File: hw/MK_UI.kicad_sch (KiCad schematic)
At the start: 19 parts, among them J11 Conn_01x03, J12 Conn_01x30, J13 Conn_02x15_Odd_Even, J14 Conn_01x06, SW1 SP-1, SW1 SP-2

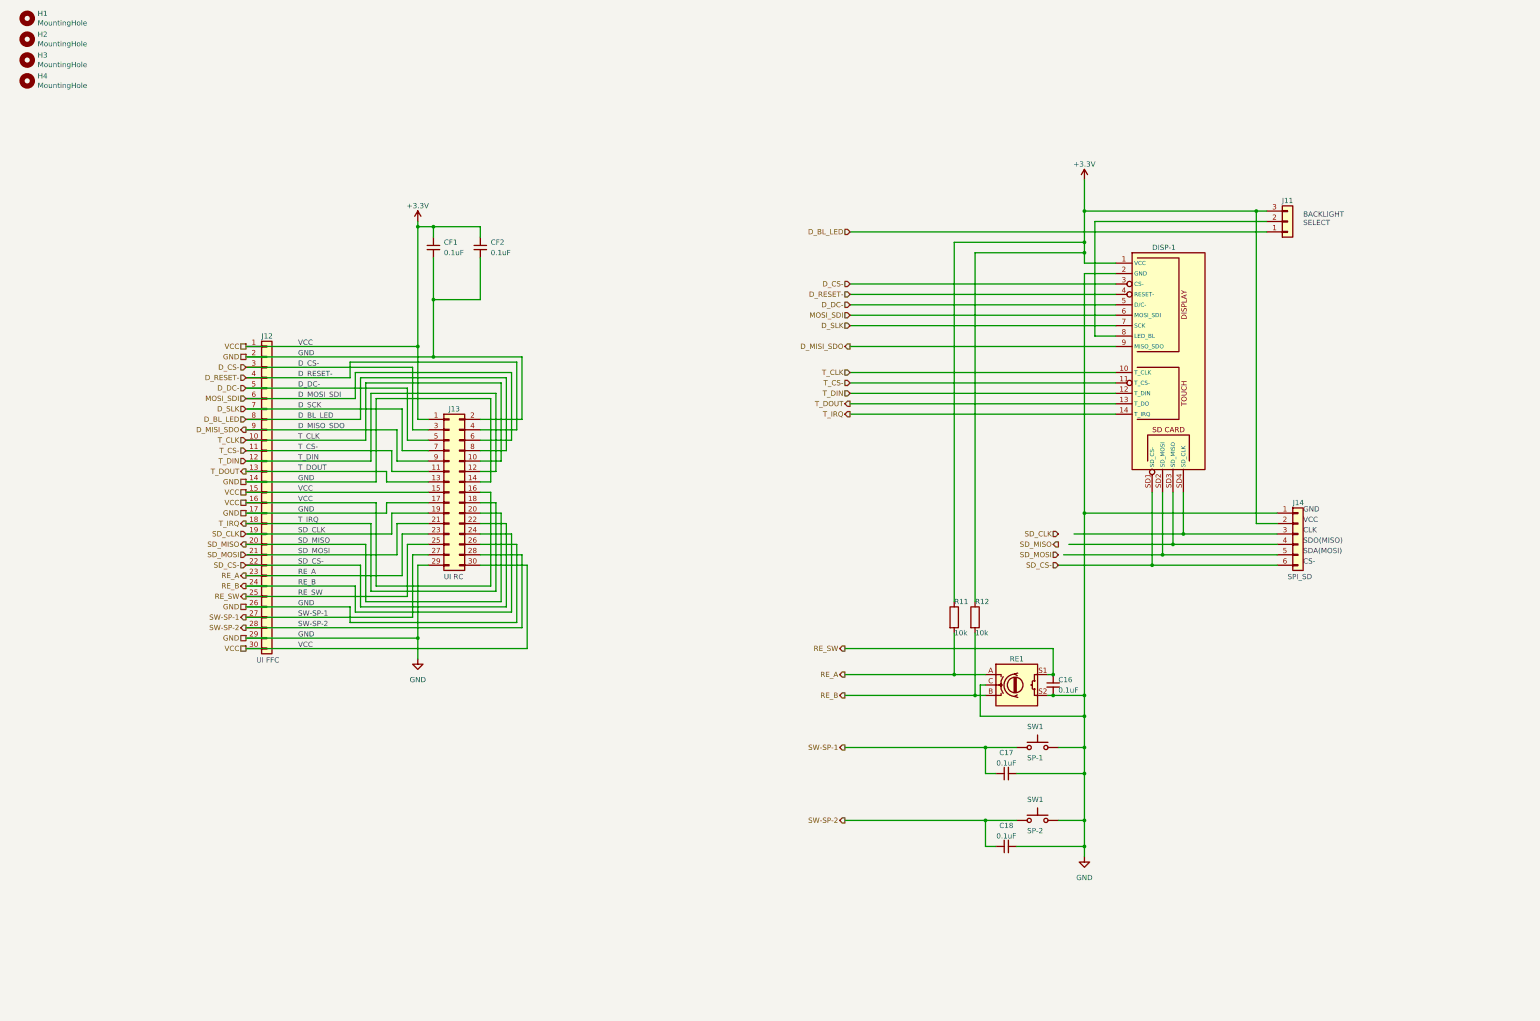
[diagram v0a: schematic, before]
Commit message: Change display backlight GPIO.
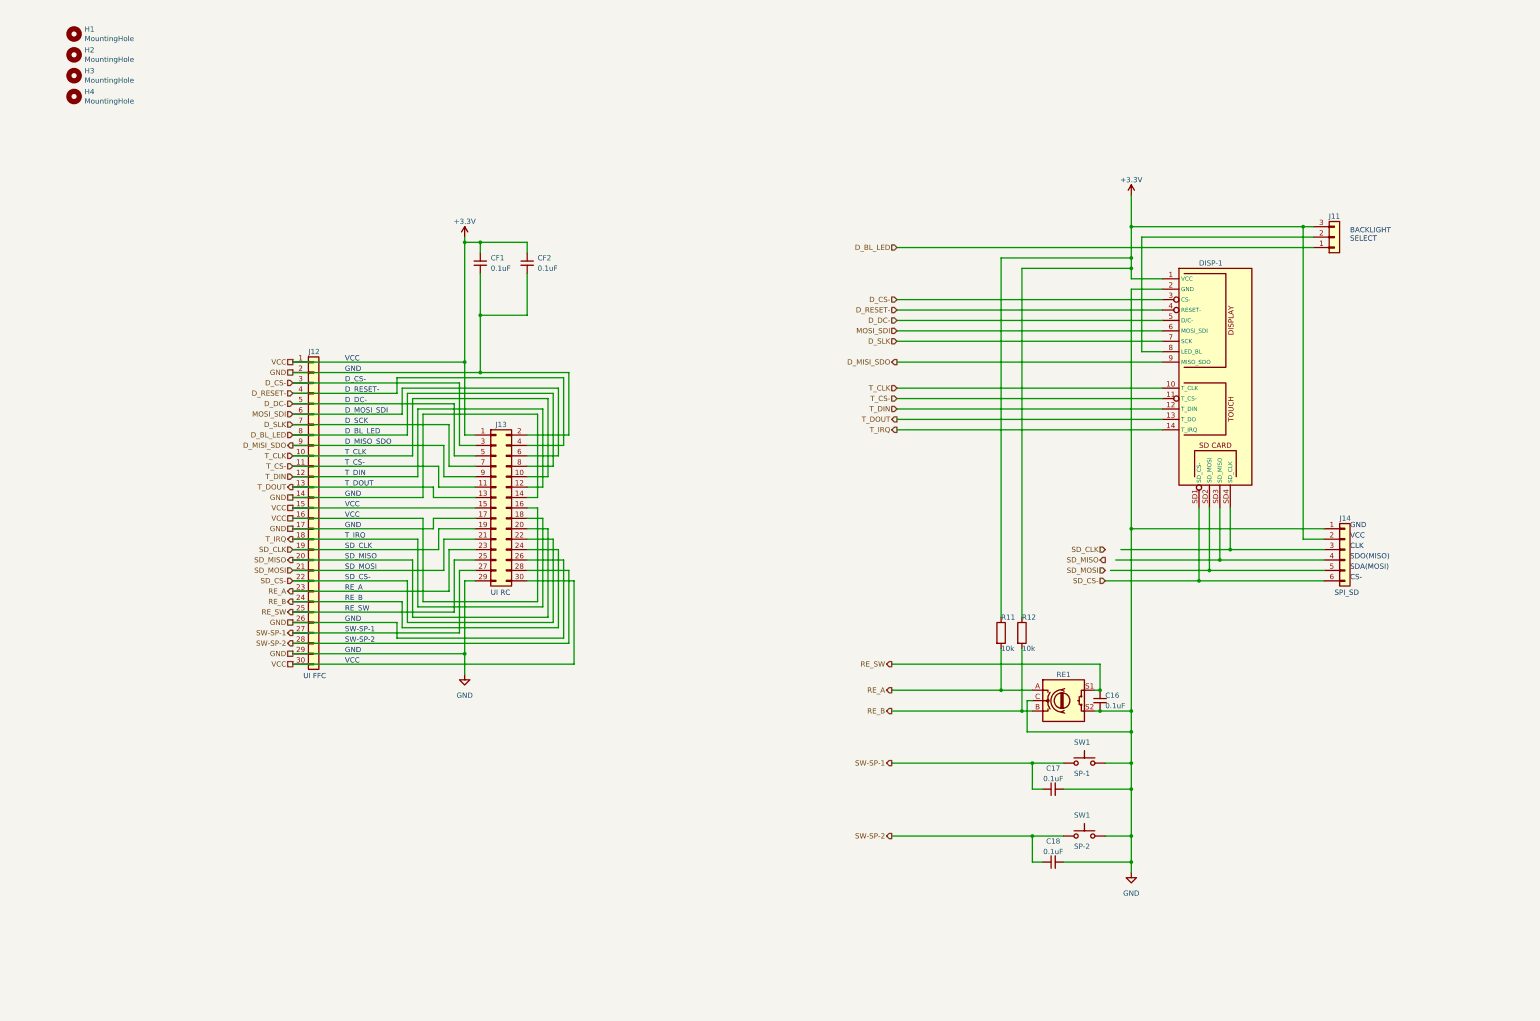
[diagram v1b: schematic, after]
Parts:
- removed SW1: SP-2, Button_Switch_SMD:SW_Push_1P1T_NO_Vertical_Wuerth_434133025816, symbol Switch:SW_Push
- removed SW1: SP-1, Button_Switch_SMD:SW_Push_1P1T_NO_Vertical_Wuerth_434133025816, symbol Switch:SW_Push
- added SW1: SP-2, Button_Switch_SMD:SW_Push_1P1T_NO_Vertical_Wuerth_434133025816, symbol Switch:SW_Push
- added SW1: SP-1, Button_Switch_SMD:SW_Push_1P1T_NO_Vertical_Wuerth_434133025816, symbol Switch:SW_Push
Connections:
- net GND: now also SW1.2, SW1.2
- net SW-SP-1: now also SW1.1
- net SW-SP-2: now also SW1.1
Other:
- title: MuKOB - User Interface -> MuKOB - UI Board

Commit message: Audio on main page. KeySounder Intf on separate board. Switch matrix via Resistors.
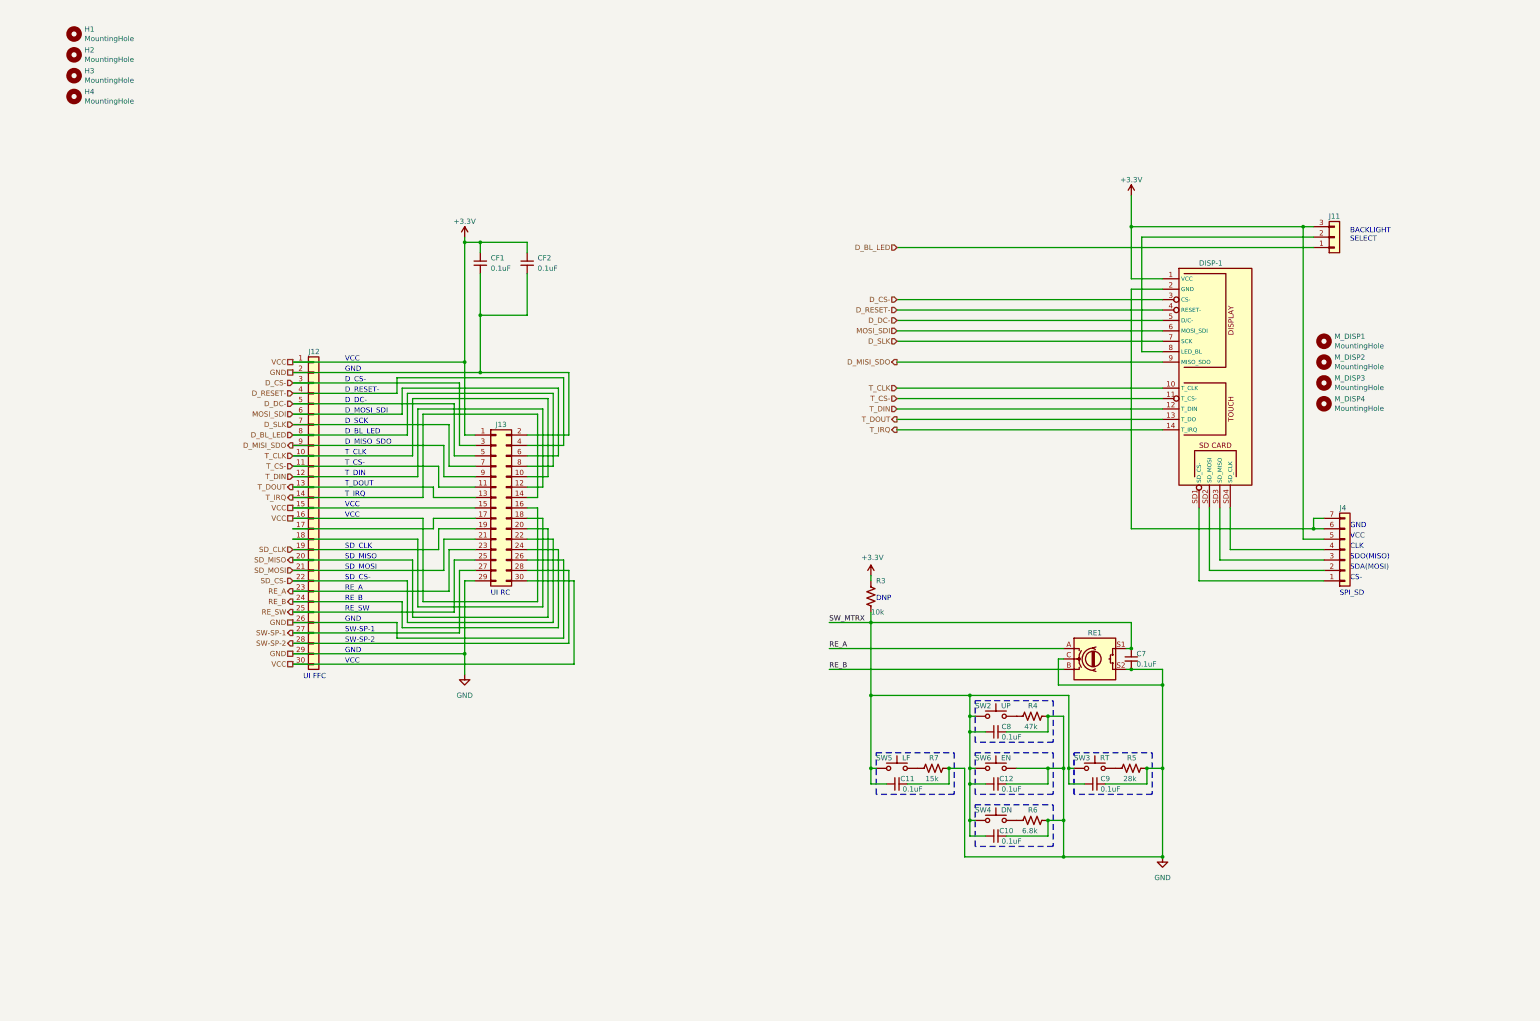
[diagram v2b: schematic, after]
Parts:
- removed C16, C17, C18: 0.1uF, symbol Device:C_Small
- removed J14: Conn_01x06, symbol Connector_Generic:Conn_01x06
- removed R11, R12: 10k, symbol Device:R
- removed SW1: SP-2, Button_Switch_SMD:SW_Push_1P1T_NO_Vertical_Wuerth_434133025816, symbol Switch:SW_Push
- removed SW1: SP-1, Button_Switch_SMD:SW_Push_1P1T_NO_Vertical_Wuerth_434133025816, symbol Switch:SW_Push
- added C10, C11, C12, C7, C8, C9: 0.1uF, symbol Device:C_Small
- added J4: Conn_01x07, symbol Connector_Generic:Conn_01x07
- added M_DISP1, M_DISP2, M_DISP3, M_DISP4: MountingHole, MountingHole:MountingHole_2.7mm_M2.5, symbol Mechanical:MountingHole
- added R3: 10k, symbol Device:R_US
- added R4: 47k, symbol Device:R_US
- added R5: 28k, symbol Device:R_US
- added R6: 6.8k, symbol Device:R_US
- added R7: 15k, symbol Device:R_US
- added SW2: UP, Button_Switch_SMD:SW_Push_1P1T_NO_Vertical_Wuerth_434133025816, symbol Switch:SW_Push
- added SW3: RT, Button_Switch_SMD:SW_Push_1P1T_NO_Vertical_Wuerth_434133025816, symbol Switch:SW_Push
- added SW4: DN, Button_Switch_SMD:SW_Push_1P1T_NO_Vertical_Wuerth_434133025816, symbol Switch:SW_Push
- added SW5: LF, Button_Switch_SMD:SW_Push_1P1T_NO_Vertical_Wuerth_434133025816, symbol Switch:SW_Push
- added SW6: EN, Button_Switch_SMD:SW_Push_1P1T_NO_Vertical_Wuerth_434133025816, symbol Switch:SW_Push
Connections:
- net +3.3V: now also J4.5 (Pin_5), R3.1
- net GND: now also C10.2, C11.2, C12.2, C7.2, C8.2, C9.2, R4.1, R5.1, R6.1, R7.1, SW6.2; no longer DISP-1.2 (GND), J12.14 (Pin_14), J12.17 (Pin_17), J13.14 (Pin_14), J13.17 (Pin_17)
- net RE_SW: no longer RE1.S1
- net SD_CS-: no longer DISP-1.SD1 (SD_CS-)
- net T_IRQ: now also J12.14 (Pin_14), J13.14 (Pin_14); no longer J12.18 (Pin_18), J13.18 (Pin_18)
- net at DISP-1.SD2 (SD_MOSI): now also J4.2 (Pin_2)
- net at DISP-1.SD3 (SD_MISO): now also J4.3 (Pin_3)
- net at DISP-1.SD4 (SD_CLK): now also J4.4 (Pin_4)
- new net: R6.2, SW4.2
- new net: DISP-1.2 (GND), J4.6 (Pin_6), J4.7 (Pin_7)
- new net: DISP-1.SD1 (SD_CS-), J4.1 (Pin_1)
- new net: R4.2, SW2.2
- new net: R7.2, SW5.2
- new net: J12.17 (Pin_17), J13.17 (Pin_17)
- new net: J12.18 (Pin_18), J13.18 (Pin_18)
- new net: R5.2, SW3.2
- new net SW_MTRX: C10.1, C11.1, C12.1, C7.1, C8.1, C9.1, R3.2, RE1.S1, SW2.1, SW3.1, SW4.1, SW5.1, SW6.1
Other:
- note added: "DNP"
- company: AESilky -> Silky-Design (AESilky)

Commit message: Reorganize onto 3 boards. Use 20pin UI connector.
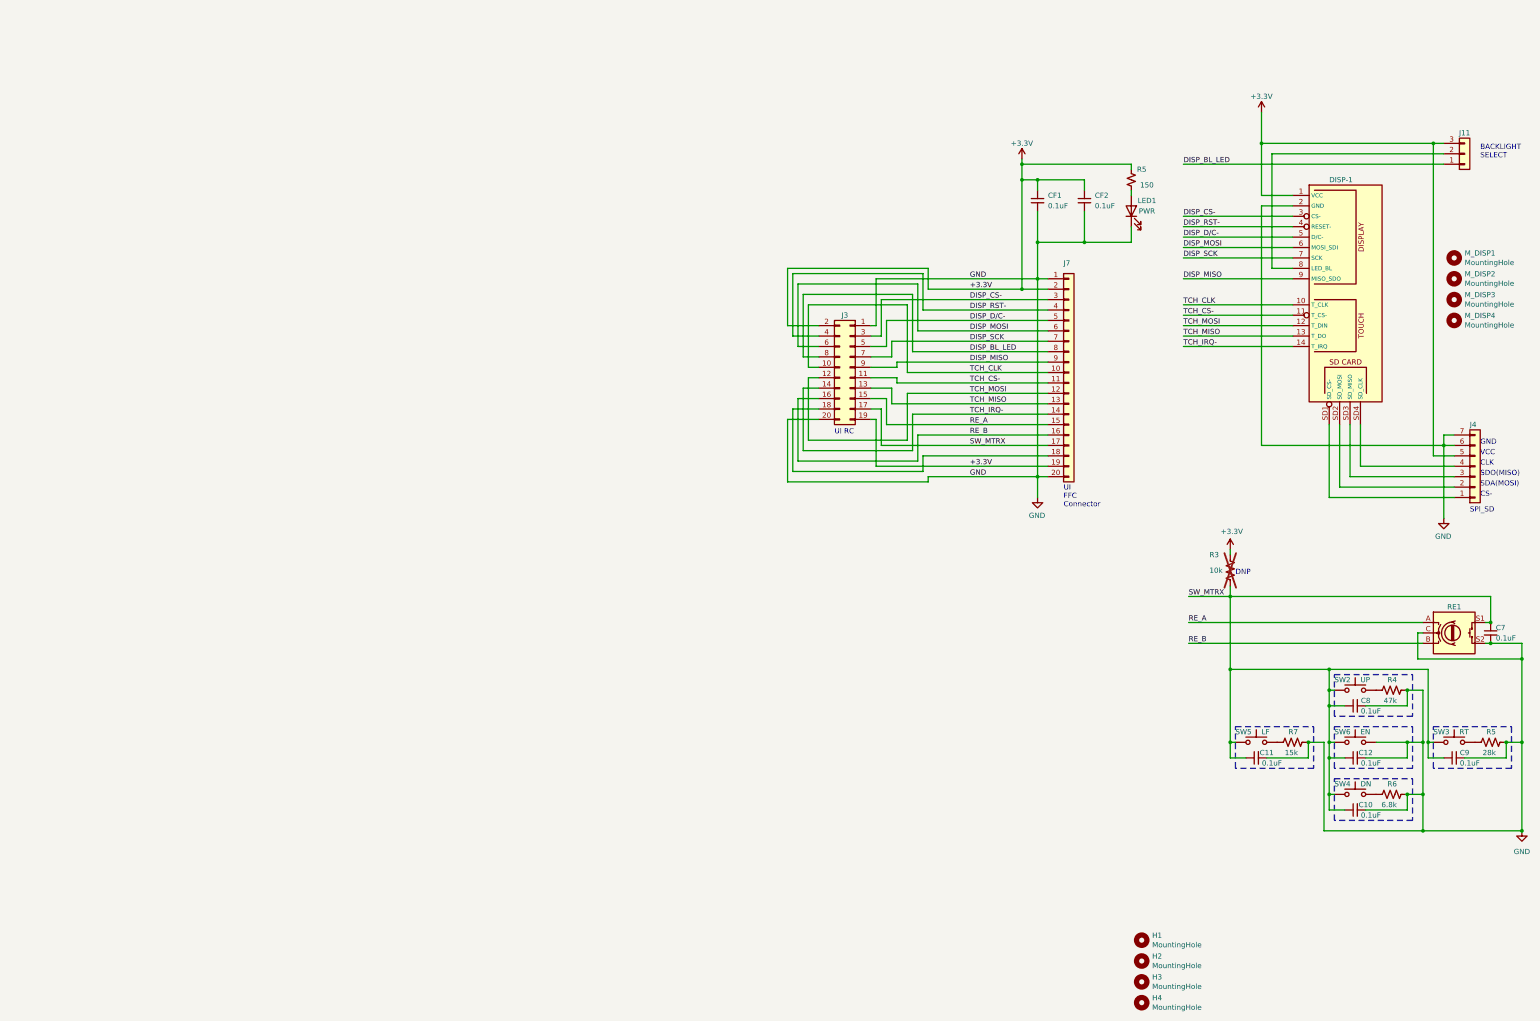
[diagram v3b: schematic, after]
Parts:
- removed J12: Conn_01x30, symbol Connector_Generic:Conn_01x30
- removed J13: Conn_02x15_Odd_Even, symbol Connector_Generic:Conn_02x15_Odd_Even
- added J3: Conn_02x10_Odd_Even, symbol Connector_Generic:Conn_02x10_Odd_Even
- added J7: Conn_01x20, symbol Connector_Generic:Conn_01x20
- added LED1: PWR, LED_THT:LED_D5.0mm, symbol Device:LED
- added R5: 150, Resistor_THT:R_Axial_DIN0207_L6.3mm_D2.5mm_P10.16mm_Horizontal, symbol Device:R_Small_US
- R3: now not fitted; now left out of the parts list
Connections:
- net +3.3V: now also J3.19 (Pin_19), J3.2 (Pin_2), J7.19 (Pin_19), J7.2 (Pin_2), R5.1
- net GND: now also DISP-1.2 (GND), J4.6 (Pin_6), J4.7 (Pin_7), J3.1 (Pin_1), J3.20 (Pin_20), J7.1 (Pin_1), J7.20 (Pin_20), LED1.1 (K)
- net RE_A: now also J3.15 (Pin_15), J7.15 (Pin_15)
- net RE_B: now also J3.16 (Pin_16), J7.16 (Pin_16)
- net SW_MTRX: now also J3.17 (Pin_17), J7.17 (Pin_17)
- net D_BL_LED renamed DISP_BL_LED
- net DISP_BL_LED: now also J3.8 (Pin_8), J7.8 (Pin_8)
- net D_CS- renamed DISP_CS-
- net DISP_CS-: now also J3.3 (Pin_3), J7.3 (Pin_3)
- net D_DC- renamed DISP_D/C-
- net DISP_D/C-: now also J3.5 (Pin_5), J7.5 (Pin_5)
- net D_MISI_SDO renamed DISP_MISO
- net DISP_MISO: now also J3.9 (Pin_9), J7.9 (Pin_9)
- net D_RESET- renamed DISP_RST-
- net DISP_RST-: now also J3.4 (Pin_4), J7.4 (Pin_4)
- net D_SLK renamed DISP_SCK
- net DISP_SCK: now also J3.7 (Pin_7), J7.7 (Pin_7)
- net MOSI_SDI renamed DISP_MOSI
- net DISP_MOSI: now also J3.6 (Pin_6), J7.6 (Pin_6)
- net T_CLK renamed TCH_CLK
- net TCH_CLK: now also J3.10 (Pin_10), J7.10 (Pin_10)
- net T_CS- renamed TCH_CS-
- net TCH_CS-: now also J3.11 (Pin_11), J7.11 (Pin_11)
- net T_DIN renamed TCH_MOSI
- net TCH_MOSI: now also J3.12 (Pin_12), J7.12 (Pin_12)
- net T_DOUT renamed TCH_MISO
- net TCH_MISO: now also J3.13 (Pin_13), J7.13 (Pin_13)
- net T_IRQ renamed TCH_IRQ-
- net TCH_IRQ-: now also J3.14 (Pin_14), J7.14 (Pin_14)
- new net: J3.18 (Pin_18), J7.18 (Pin_18)
- new net: LED1.2 (A), R5.2
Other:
- note added: "UI FFC Connector"
- note removed: "D_BL_LED"
- note removed: "D_CS-"
- note removed: "D_DC-"
- note removed: "D_MISO_SDO"
- note removed: "D_MOSI_SDI"
- note removed: "D_RESET-"
- note removed: "D_SCK"
- note removed: "RE_A"
- note removed: "RE_B"
- note removed: "RE_SW"
- note removed: "SD_CLK"
- note removed: "SD_CS-"
- note removed: "SD_MISO"
- note removed: "SD_MOSI"
- note removed: "SW-SP-1"
- note removed: "SW-SP-2"
- note removed: "T_CLK"
- note removed: "T_CS-"
- note removed: "T_DIN"
- note removed: "T_DOUT"
- note removed: "T_IRQ"
- note removed: "UI FFC"
- moved on the sheet: C10, C11, C12, C7, C8, C9, CF1, CF2, DISP-1, H1, H2, H3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

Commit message: Electrical checks complete.
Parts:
- removed J4: Conn_01x07, symbol Connector_Generic:Conn_01x07
- removed M_DISP4: MountingHole, MountingHole:MountingHole_2.7mm_M2.5, symbol Mechanical:MountingHole
- added J3: SW_MATRIX, symbol Connector_Generic:Conn_01x05
- added R5: 100, Resistor_THT:R_Axial_DIN0207_L6.3mm_D2.5mm_P10.16mm_Horizontal, symbol Device:R_Small_US
- added TP3: Test_Point_01, symbol Test_point_Jump:TP_01
- M_DISP1: value MountingHole -> MountingHole-2_8
- M_DISP2: value MountingHole -> MountingHole-3_5
- M_DISP3: value MountingHole -> MountingHole-4_0
- R3: now fitted
- R5: value 150 -> 100
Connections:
- net +3.3V: now also J3.1 (Pin_1), J7.1 (Pin_1), J3.5 (Pin_5), R5.1; no longer J11.3 (Pin_3), J3.2 (Pin_2), J7.2 (Pin_2)
- net GND: now also J3.2 (Pin_2), J7.2 (Pin_2), J3.1 (Pin_1); no longer J3.1 (Pin_1), J7.1 (Pin_1)
- net RE_A: now also J3.3 (Pin_3)
- net RE_B: now also J3.2 (Pin_2)
- net SW_MTRX: now also J3.4 (Pin_4)
- net open18: now reaches J3.18 (Pin_18), J7.18 (Pin_18)
- net open18: now also TP3.1 (Pin_1)
- new net: J11.3 (Pin_3), R5.2
- no-connect marks 0 -> 4
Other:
- note added: "BACKLIGHT PWR SELECT"
- note added: "DNP (On MB)"
- note removed: "BACKLIGHT SELECT"
- note removed: "CLK"
- note removed: "CS-"
- note removed: "DNP"
- note removed: "GND"
- note removed: "SDA(MOSI)"
- note removed: "SDO(MISO)"
- note removed: "SPI_SD"
- note removed: "VCC"
- moved on the sheet: C10, C11, C12, C7, C8, C9, CF1, CF2, DISP-1, H1, H2, H3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

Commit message: Schematic updates. Reorg components between boards. 20 pin ribbon.
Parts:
- removed J3: Conn_02x10_Odd_Even, symbol Connector_Generic:Conn_02x10_Odd_Even
- removed J7: Conn_01x20, symbol Connector_Generic:Conn_01x20
- removed TP3: Test_Point_01, symbol Test_point_Jump:TP_01
- added J16: UI 20-Ribbon, symbol Connector_Generic:Conn_02x14_Odd_Even
- added J2: Conn_01x20, symbol Connector_Generic:Conn_01x20
- added R5: 2.2k, symbol Device:R_US
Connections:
- net +3.3V: now also J16.11 (Pin_11), J16.2 (Pin_2), J2.1 (Pin_1), J2.20 (Pin_20); no longer J3.5 (Pin_5)
- net DISP_BL_LED: now also J16.16 (Pin_16), J2.8 (Pin_8)
- net DISP_CS-: now also J16.6 (Pin_6), J2.3 (Pin_3)
- net DISP_D/C-: now also J16.10 (Pin_10), J2.5 (Pin_5)
- net DISP_MISO: now also J16.18 (Pin_18), J2.9 (Pin_9)
- net DISP_MOSI: now also J16.12 (Pin_12), J2.6 (Pin_6)
- net DISP_RST-: now also J16.8 (Pin_8), J2.4 (Pin_4)
- net DISP_SCK: now also J16.14 (Pin_14), J2.7 (Pin_7)
- net GND: now also J3.2 (Pin_2), J3.5 (Pin_5), RE1.S1, J16.3 (Pin_3), J16.4 (Pin_4), J16.7 (Pin_7), J2.16 (Pin_16), J2.18 (Pin_18), J2.2 (Pin_2), R5.1; no longer J3.1 (Pin_1), RE1.S2, SW6.2
- net RE_A: now also J3.1 (Pin_1), J16.1 (Pin_1), J2.15 (Pin_15); no longer J3.3 (Pin_3)
- net RE_B: now also J3.3 (Pin_3), J16.5 (Pin_5), J2.17 (Pin_17); no longer J3.2 (Pin_2)
- net SW_MTRX: now also RE1.S2, J16.9 (Pin_9), J2.19 (Pin_19); no longer RE1.S1
- net TCH_CS-: now also J16.13 (Pin_13), J16.22 (Pin_22), J2.11 (Pin_11)
- net TCH_IRQ-: now also J16.19 (Pin_19), J16.28 (Pin_28), J2.14 (Pin_14)
- new net: R5.2, SW6.2
- new net SD_TP_EX_MISO: J16.17 (Pin_17), J16.26 (Pin_26), J2.13 (Pin_13)
- new net SD_TP_EX_MOSI: J16.15 (Pin_15), J16.24 (Pin_24), J2.12 (Pin_12)
- new net SD_TP_EX_SCK: J16.20 (Pin_20), J2.10 (Pin_10)
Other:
- note added: "UI 20-FFC"
- note removed: "UI FFC Connector"
- note removed: "UI RC"
- moved on the sheet: CF1, CF2, J3, LED1, R5
